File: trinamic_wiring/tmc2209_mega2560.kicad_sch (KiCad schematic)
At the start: 4 parts, among them M1 Stepper_Motor_QSH2818-32-07-0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

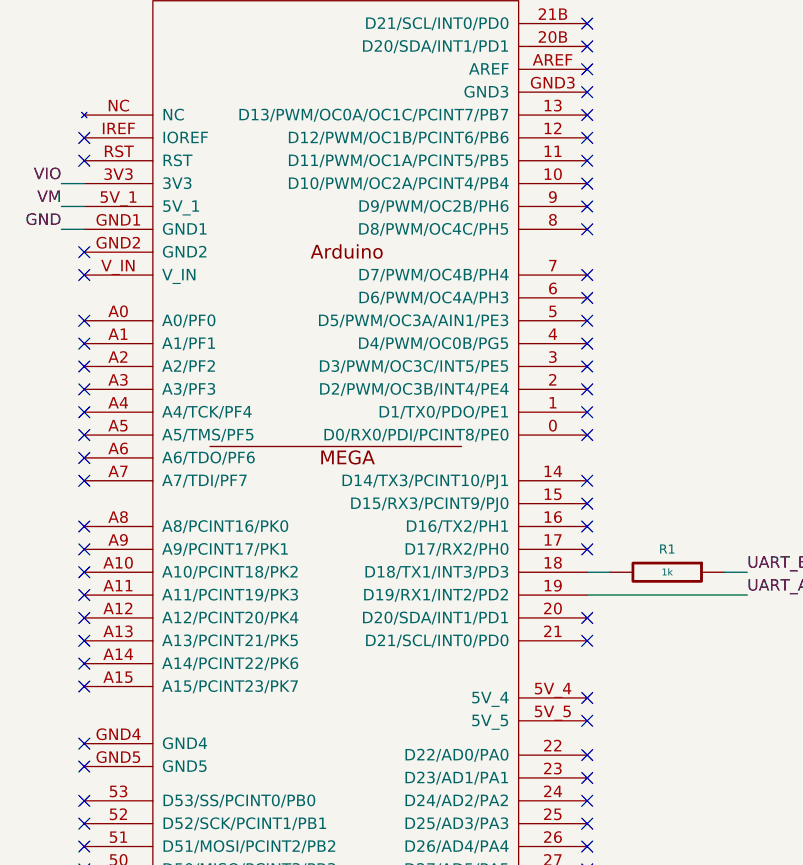
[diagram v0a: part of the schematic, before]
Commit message: Mega VIO should connect to 5V not 3.3V
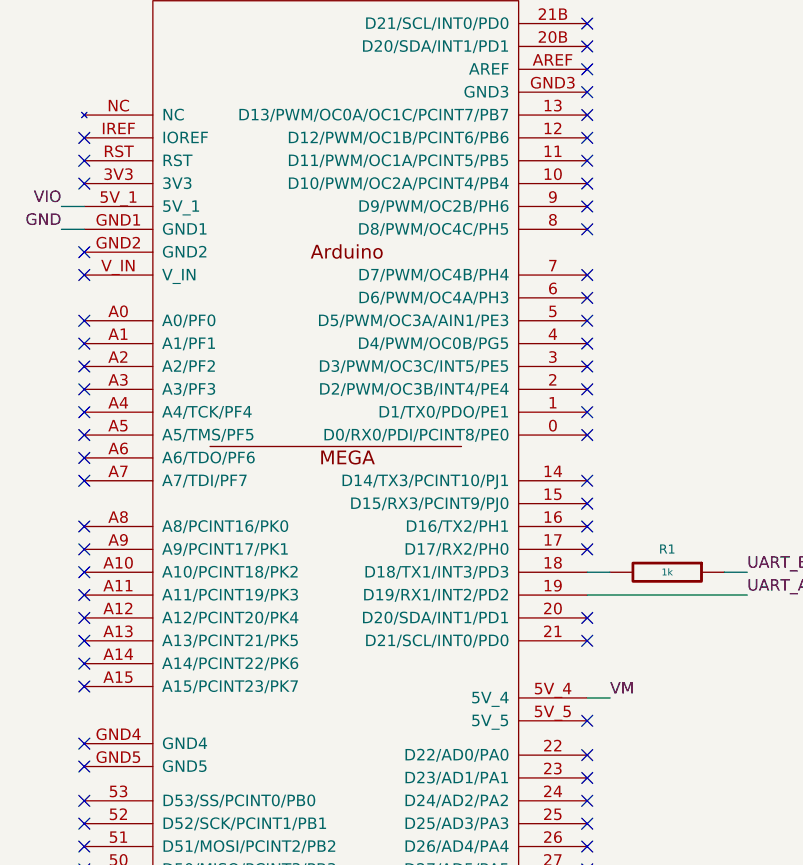
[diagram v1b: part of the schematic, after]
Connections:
- net VIO: now also ARDUINO1.5V_1; no longer ARDUINO1.3V3
- net VM: now also ARDUINO1.5V_4; no longer ARDUINO1.5V_1
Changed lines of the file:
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@@
   (no_connect (at 87.63 74.93))
   (no_connect (at 31.75 74.93))
-  (no_connect (at 87.63 121.92))
   (no_connect (at 31.75 102.87))
   (no_connect (at 31.75 97.79))
@@
   (no_connect (at 31.75 107.95))
   (no_connect (at 87.63 162.56))
+  (no_connect (at 31.75 64.77))
   (no_connect (at 137.16 104.14))
   (no_connect (at 31.75 105.41))
@@
     (stroke (width 0) (type default) (color 0 0 0 0))
   )
-  (wire (pts (xy 31.75 64.77) (xy 29.21 64.77))
-    (stroke (width 0) (type default) (color 0 0 0 0))
-  )
   (wire (pts (xy 105.41 107.95) (xy 102.87 107.95))
     (stroke (width 0) (type default) (color 0 0 0 0))
@@
   )
   (wire (pts (xy 134.62 96.52) (xy 137.16 96.52))
+    (stroke (width 0) (type default) (color 0 0 0 0))
+  )
+  (wire (pts (xy 87.63 121.92) (xy 90.17 121.92))
     (stroke (width 0) (type default) (color 0 0 0 0))
   )
@@
     (effects (font (size 1.27 1.27)) (justify left bottom))
   )
-  (label "VIO" (at 29.21 64.77 180)
+  (label "VIO" (at 29.21 67.31 180)
     (effects (font (size 1.27 1.27)) (justify right bottom))
   )
@@
     (effects (font (size 1.27 1.27)) (justify right bottom))
   )
-  (label "VM" (at 29.21 67.31 180)
-    (effects (font (size 1.27 1.27)) (justify right bottom))
+  (label "VM" (at 90.17 121.92 0)
+    (effects (font (size 1.27 1.27)) (justify left bottom))
   )
   (label "A-" (at 170.18 97.79 0)

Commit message: Update version
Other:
- company: (none) -> Janelia Research Campus
- title: TMC2209 MEGA2560 -> Trinamic Wiring

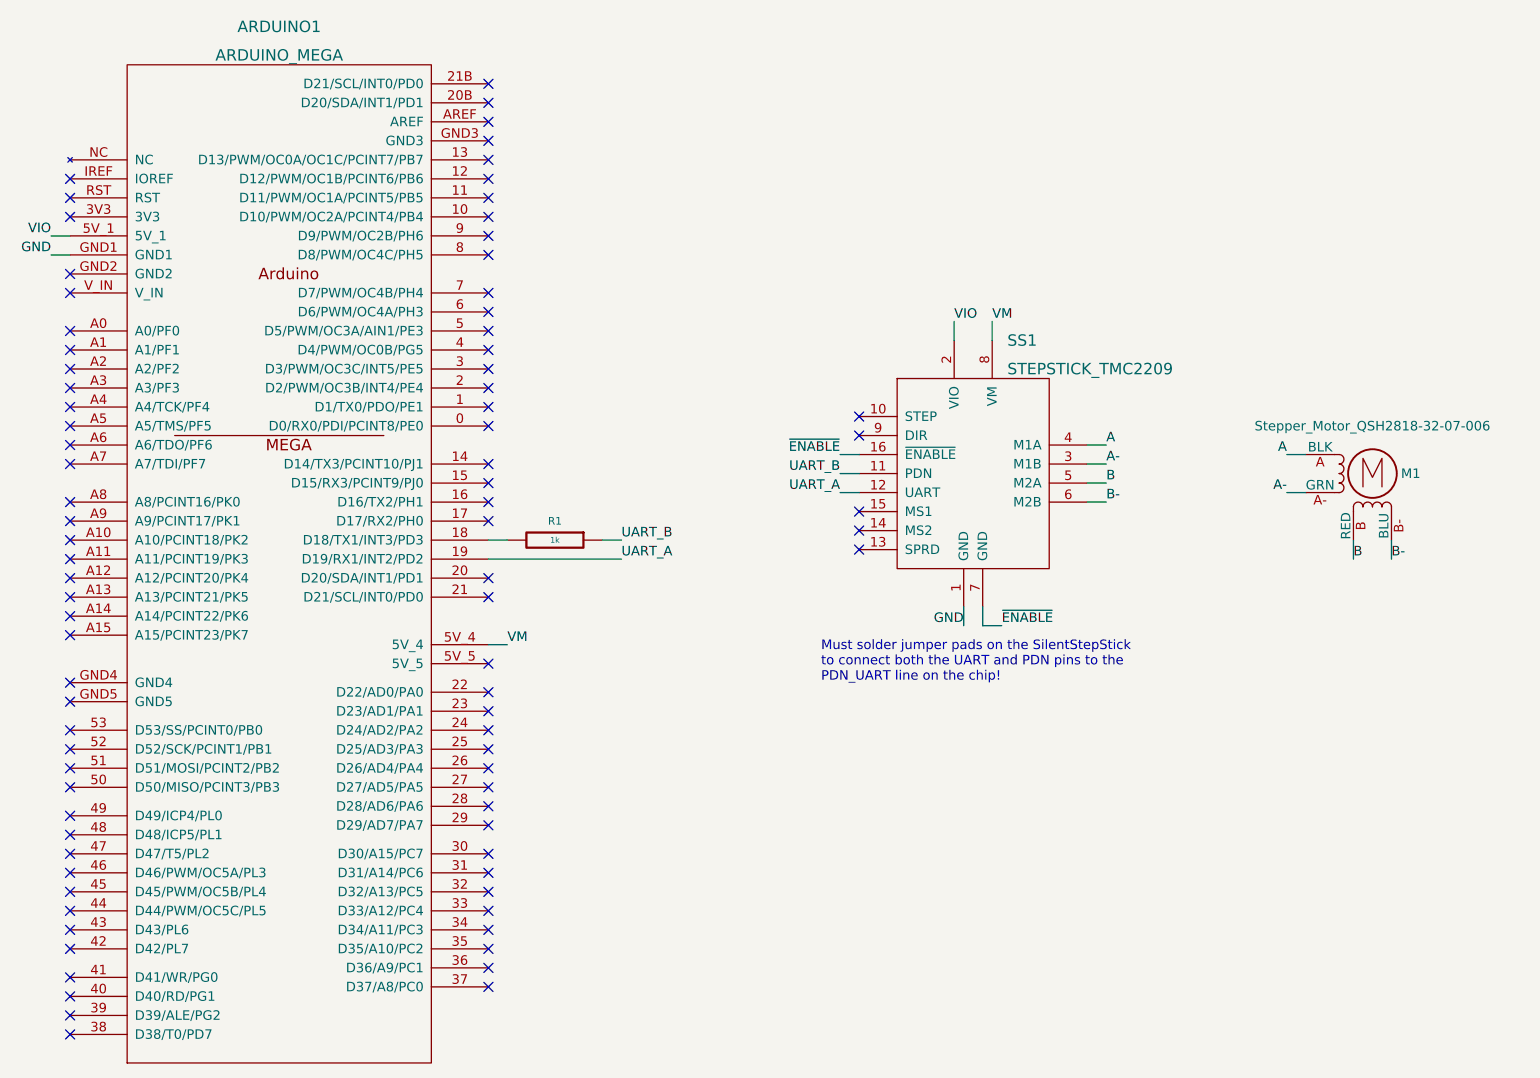
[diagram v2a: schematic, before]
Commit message: Make updates for new version of TMC2209 library
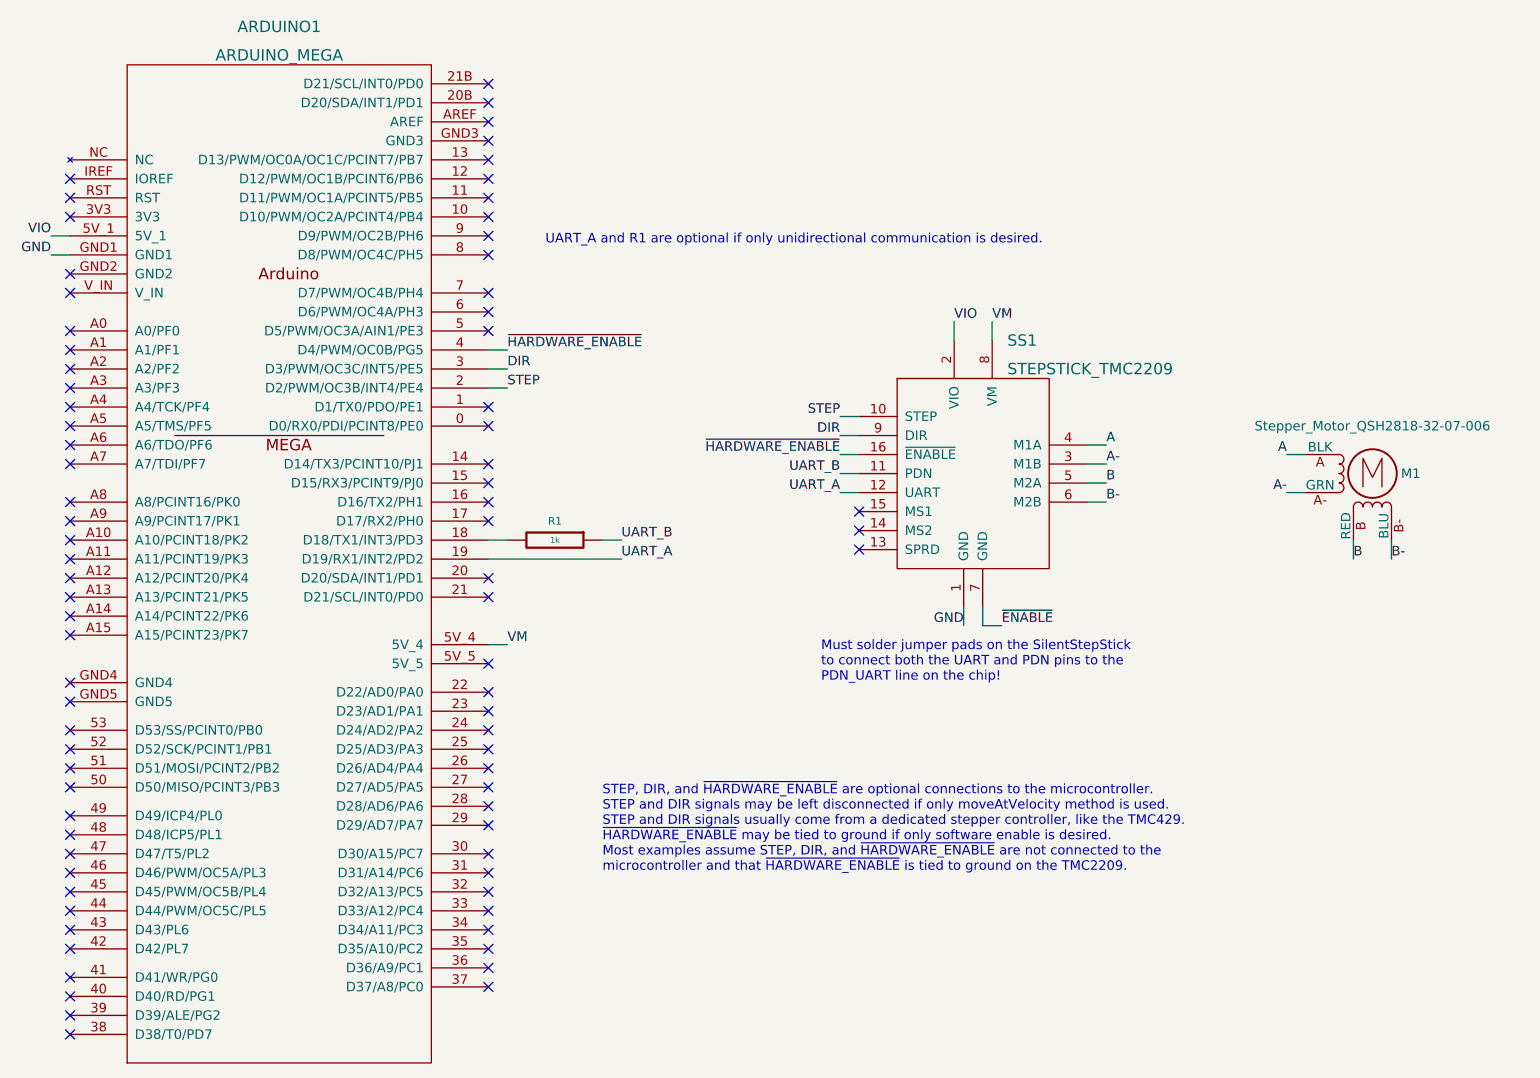
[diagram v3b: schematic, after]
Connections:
- net ~{ENABLE}: no longer SS1.16 (~{ENABLE})
- net STEP: now reaches SS1.10 (STEP)
- net STEP: now also ARDUINO1.2 (D2/PWM/OC3B/INT4/PE4)
- net DIR: now reaches SS1.9 (DIR)
- net DIR: now also ARDUINO1.3 (D3/PWM/OC3C/INT5/PE5)
- net ~{HARDWARE_ENABLE}: now reaches ARDUINO1.4 (D4/PWM/OC0B/PG5)
- net ~{HARDWARE_ENABLE}: now also SS1.16 (~{ENABLE})
- no-connect marks 85 -> 80
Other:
- note added: "STEP, DIR, and ~{HARDWARE_ENABLE} are optional connections to the microcontroller. STEP and DIR signals may be left disconnected if only moveAtVelocity method is used. STEP and DIR signals usually come from a dedicated stepper controller, like the TMC429. ~{HARDWARE_ENABLE} may be tied to ground if only software enable is desired. Most examples assume STEP, DIR, and ~{HARDWARE_ENABLE} are not con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"
- note added: "UART_A and R1 are optional if only unidirectional communication is desired."
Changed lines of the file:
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@@
   (no_connect (at 31.75 87.63))
   (no_connect (at 31.75 95.25))
-  (no_connect (at 137.16 91.44))
-  (no_connect (at 87.63 82.55))
   (no_connect (at 87.63 100.33))
   (no_connect (at 31.75 173.99))
@@
   (no_connect (at 31.75 118.11))
   (no_connect (at 137.16 106.68))
-  (no_connect (at 87.63 85.09))
   (no_connect (at 87.63 140.97))
   (no_connect (at 87.63 124.46))
@@
   (no_connect (at 137.16 104.14))
   (no_connect (at 31.75 105.41))
-  (no_connect (at 87.63 87.63))
   (no_connect (at 31.75 140.97))
   (no_connect (at 31.75 133.35))
-  (no_connect (at 137.16 93.98))
   (no_connect (at 31.75 127))
   (no_connect (at 87.63 154.94))
@@
     (stroke (width 0) (type default))
   )
+  (wire (pts (xy 90.17 85.09) (xy 87.63 85.09))
+    (stroke (width 0) (type default))
+  )
   (wire (pts (xy 90.17 107.95) (xy 87.63 107.95))
     (stroke (width 0) (type default))
@@
     (stroke (width 0) (type default))
   )
+  (wire (pts (xy 90.17 82.55) (xy 87.63 82.55))
+    (stroke (width 0) (type default))
+  )
   (wire (pts (xy 167.64 100.33) (xy 170.18 100.33))
     (stroke (width 0) (type default))
@@
     (stroke (width 0) (type default))
   )
+  (wire (pts (xy 134.62 91.44) (xy 137.16 91.44))
+    (stroke (width 0) (type default))
+  )
   (wire (pts (xy 134.62 96.52) (xy 137.16 96.52))
     (stroke (width 0) (type default))
@@
     (stroke (width 0) (type default))
   )
+  (wire (pts (xy 134.62 93.98) (xy 137.16 93.98))
+    (stroke (width 0) (type default))
+  )
   (wire (pts (xy 154.94 78.74) (xy 154.94 81.28))
     (stroke (width 0) (type default))
+  )
+  (wire (pts (xy 90.17 87.63) (xy 87.63 87.63))
+    (stroke (width 0) (type default))
+  )
+  (text "STEP, DIR, and ~{HARDWARE_ENABLE} are optional connections to the microcontroller.\nSTEP and DIR signals may be left disconnected if only moveAtVelocity method is used.\nSTEP and DIR signals usually come from a dedicated stepper controller, like the TMC429.\n~{HARDWARE_ENABLE} may be tied to ground if only software enable is desired.\nMost examples assume STEP, DIR, and ~{HARDWARE_ENABLE} are not connected to the\nmicrocontroller and that ~{HARDWARE_ENABLE} is tied to ground on the TMC2209."
+    (at 102.87 152.4 0)
+    (effects (font (size 1.27 1.27)) (justify left bottom))
+  )
+  (text "UART_A and R1 are optional if only unidirectional communication is desired."
+    (at 95.25 68.58 0)
+    (effects (font (size 1.27 1.27)) (justify left bottom))
   )
   (text "Must solder jumper pads on the SilentStepStick\nto connect both the UART and PDN pins to the\nPDN_UART line on the chip!"
@@
     (effects (font (size 1.27 1.27)) (justify right bottom))
   )
+  (label "~{HARDWARE_ENABLE}" (at 90.17 82.55 0) (fields_autoplaced)
+    (effects (font (size 1.27 1.27)) (justify left bottom))
+  )
   (label "UART_B" (at 105.41 107.95 0) (fields_autoplaced)
     (effects (font (size 1.27 1.27)) (justify left bottom))
@@
     (effects (font (size 1.27 1.27)) (justify left bottom))
   )
-  (label "~{ENABLE}" (at 134.62 96.52 180) (fields_autoplaced)
+  (label "~{HARDWARE_ENABLE}" (at 134.62 96.52 180) (fields_autoplaced)
     (effects (font (size 1.27 1.27)) (justify right bottom))
   )
@@
     (effects (font (size 1.27 1.27)) (justify left bottom))
   )
+  (label "DIR" (at 90.17 85.09 0) (fields_autoplaced)
+    (effects (font (size 1.27 1.27)) (justify left bottom))
+  )
   (label "B" (at 170.18 100.33 0) (fields_autoplaced)
     (effects (font (size 1.27 1.27)) (justify left bottom))
@@
     (effects (font (size 1.27 1.27)) (justify right bottom))
   )
+  (label "DIR" (at 134.62 93.98 180) (fields_autoplaced)
+    (effects (font (size 1.27 1.27)) (justify right bottom))
+  )
   (label "GND" (at 29.21 69.85 180) (fields_autoplaced)
     (effects (font (size 1.27 1.27)) (justify right bottom))
   )
+  (label "STEP" (at 90.17 87.63 0) (fields_autoplaced)
+    (effects (font (size 1.27 1.27)) (justify left bottom))
+  )
   (label "VM" (at 90.17 121.92 0) (fields_autoplaced)
     (effects (font (size 1.27 1.27)) (justify left bottom))
   )
+  (label "STEP" (at 134.62 91.44 180) (fields_autoplaced)
+    (effects (font (size 1.27 1.27)) (justify right bottom))
+  )
   (label "A-" (at 170.18 97.79 0) (fields_autoplaced)

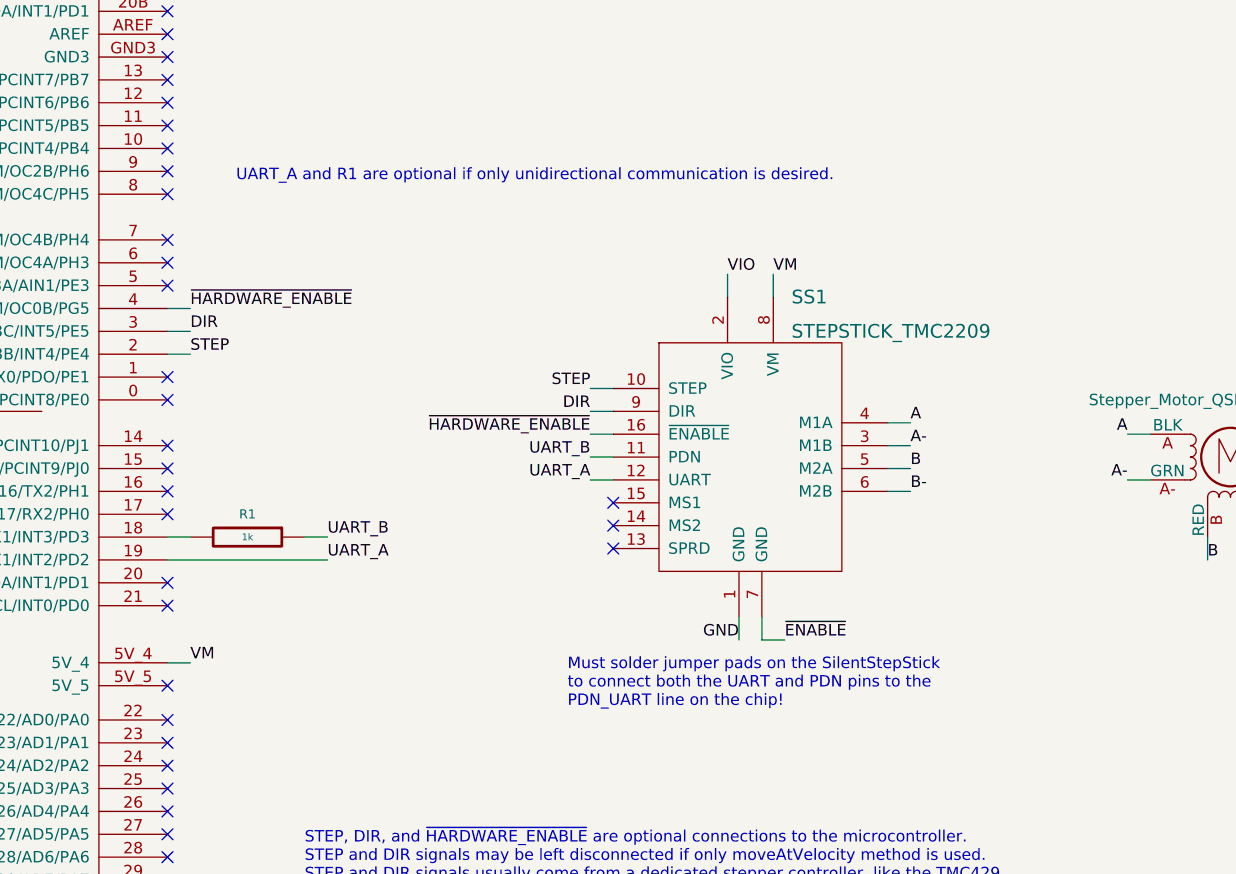
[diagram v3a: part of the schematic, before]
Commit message: Update wiring for TMC2209 v9
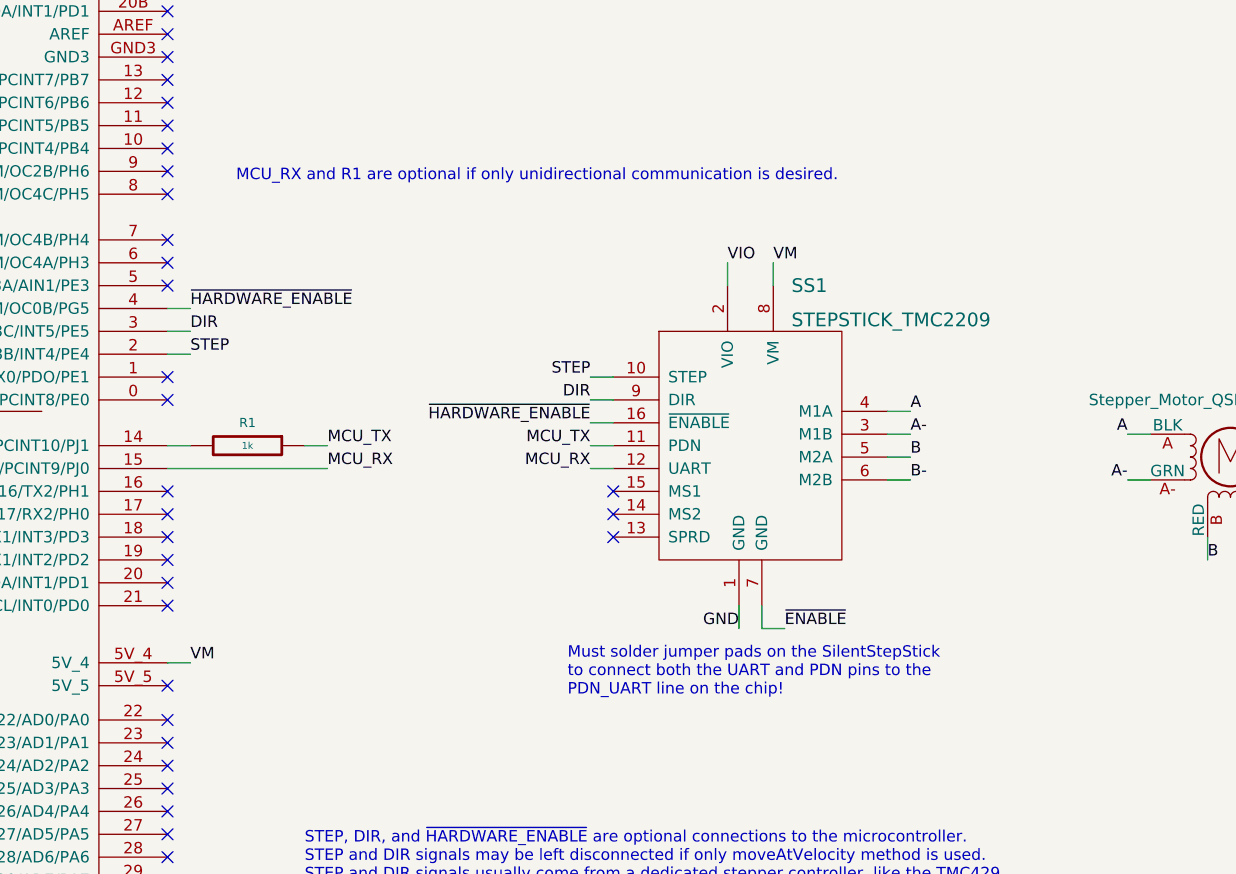
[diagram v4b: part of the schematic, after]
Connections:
- net at R1.2: now also ARDUINO1.14 (D14/TX3/PCINT10/PJ1); no longer ARDUINO1.18 (D18/TX1/INT3/PD3)
- net MCU_RX: now reaches ARDUINO1.15 (D15/RX3/PCINT9/PJ0)
- net MCU_RX: now also SS1.12 (UART)
- net UART_A: no longer names the net of ARDUINO1.19 (D19/RX1/INT2/PD2)
- net UART_A: no longer SS1.12 (UART)
- net UART_B renamed MCU_TX
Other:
- note added: "MCU_RX and R1 are optional if only unidirectional communication is desired."
- note removed: "UART_A and R1 are optional if only unidirectional communication is desired."
- moved on the sheet: R1, SS1
